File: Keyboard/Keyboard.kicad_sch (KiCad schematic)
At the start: 134 parts, among them SW1 Escape, SW10 8/*, SW11 9/(, SW12 0/), SW13 -/_, SW14 =/+, SW15 Delete, SW16 Tab, SW17 Q, SW18 W, SW19 E, SW2 `/~, SW20 R, SW21 T, SW22 Y, SW23 U, SW24 I, SW25 O, SW26 P, SW27 [/{, SW28 ]/}, SW29 \/|, SW3 1/!, SW30 Caps, SW31 A, SW32 S, SW33 D, SW34 F, SW35 G, SW36 H, SW37 J, SW38 K, SW39 L, SW4 2/@, SW40 ;/:, SW41 '/", SW42 Return, SW43 L Shift, SW44 Z, SW45 X, SW46 C, SW47 V, SW48 B, SW49 N, SW5 3/#, SW50 M, SW51 ,/<, SW52 ./>, SW53 //?, SW54 R Shift, SW55 L Control, SW56 L Alt, SW57 L Command, SW58 Space, SW59 R Command, SW6 4/$, SW60 R Alt, SW61 Up, SW62 Left, SW63 Down, SW64 Right, SW65 R Control, SW7 5/%, SW8 6/^, SW9 7/&

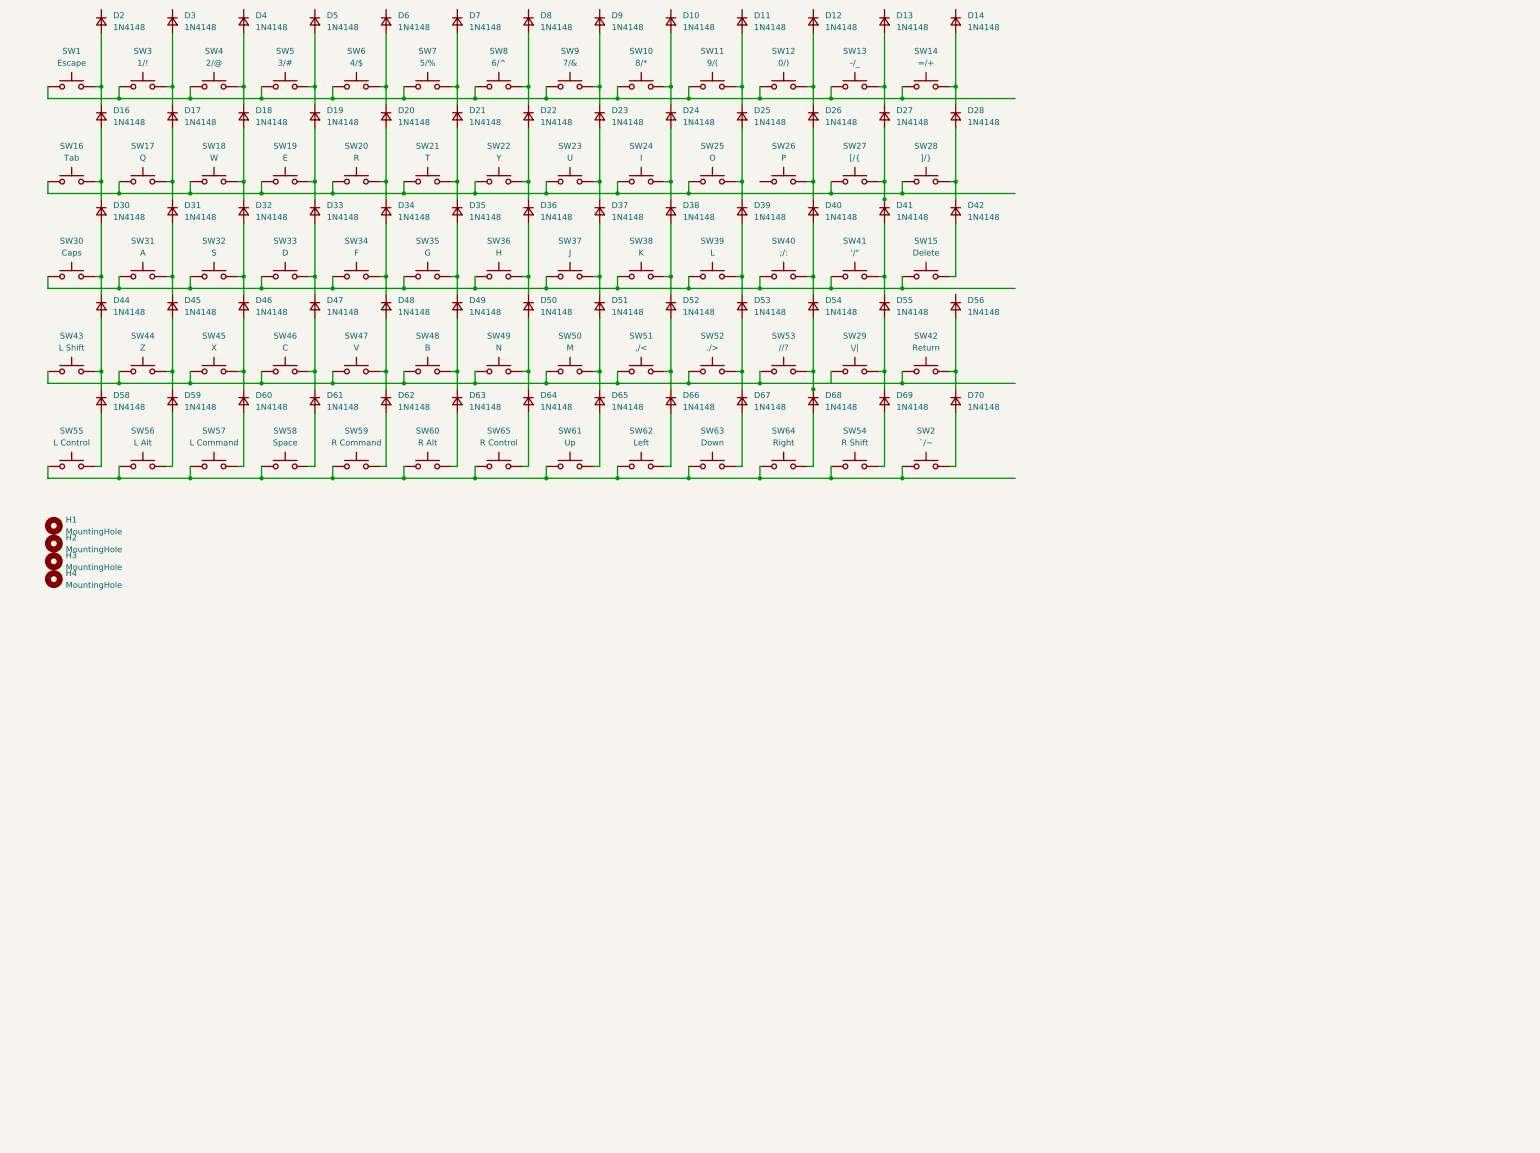
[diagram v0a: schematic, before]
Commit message: mostly updating keyboard
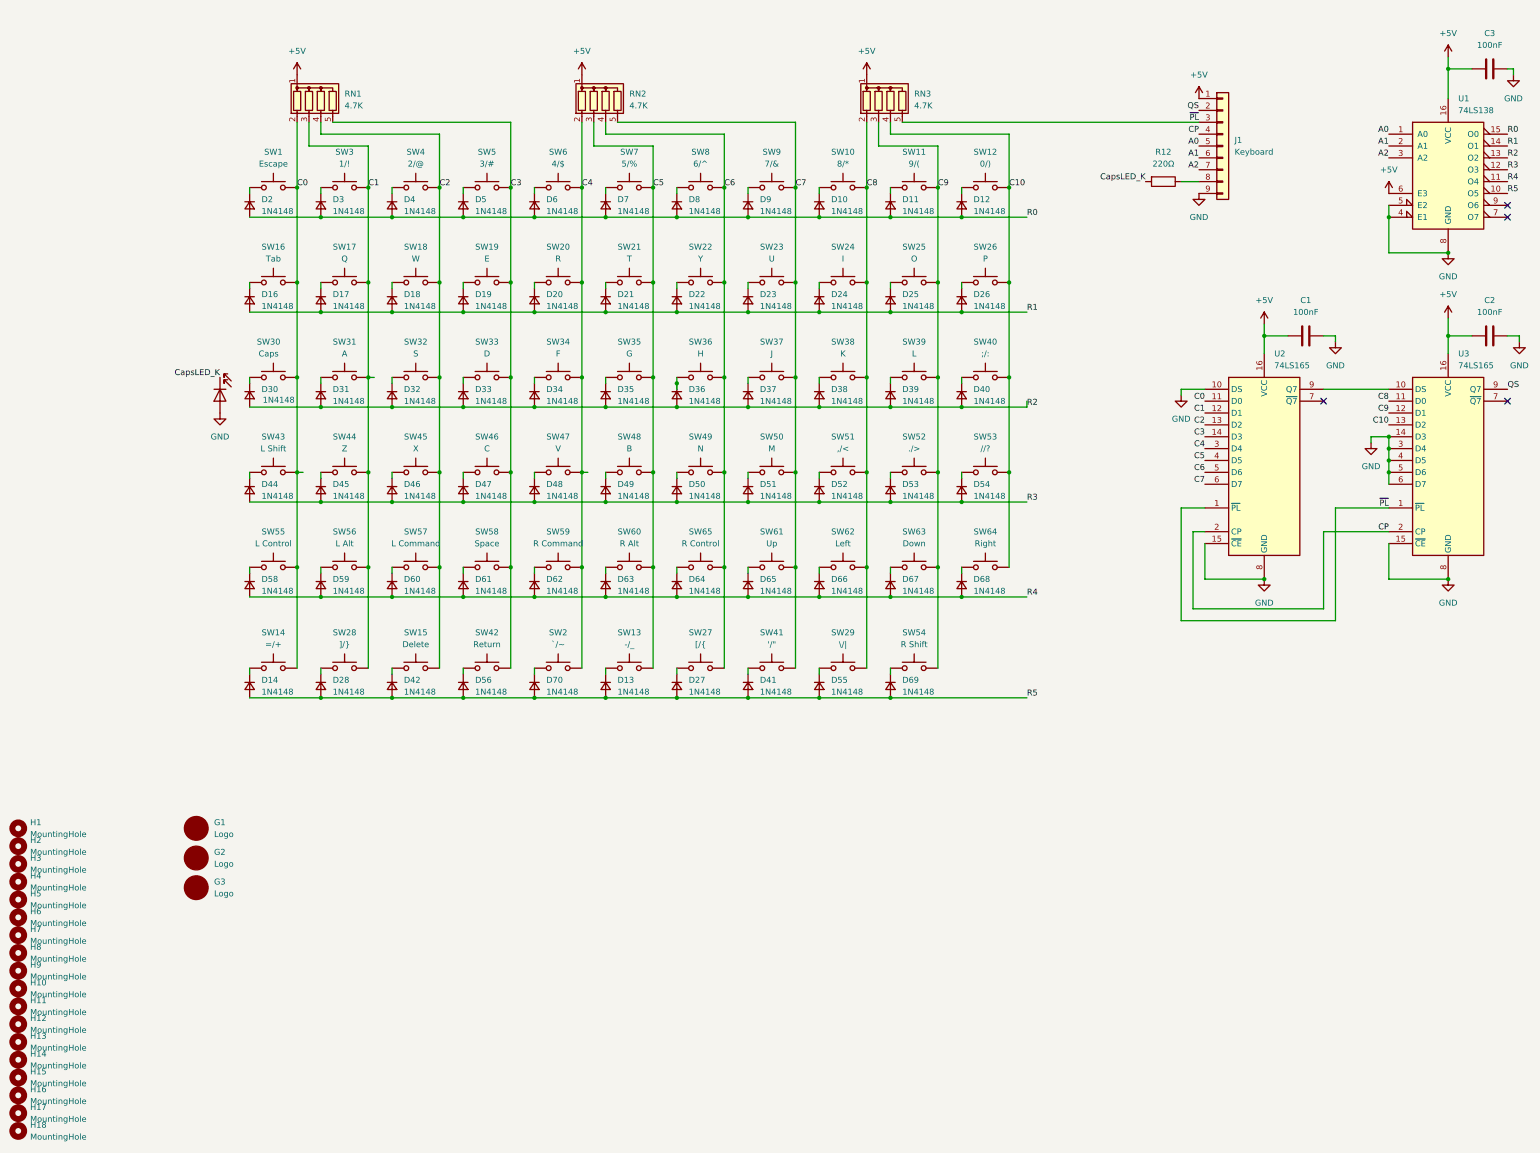
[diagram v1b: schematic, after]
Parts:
- added C1, C2, C3: 100nF, 0-Footprints:C_Disc_D5.0mm_W2.5mm_P5.00mm, symbol Device:C
- added G1: Logo, 0-Footprints:Crank, symbol 0-Symbols:Logo
- added G2: Logo, Symbol:OSHW-Logo2_7.3x6mm_SilkScreen, symbol 0-Symbols:Logo
- added G3: Logo, 0-Footprints:crankery_small, symbol 0-Symbols:Logo
- added H10, H11, H12, H13, H14, H15, H16, H17, H18, H5, H6, H7, H8, H9: MountingHole, 0-Footprints:MountingHole_2.1mm, symbol Mechanical:MountingHole
- added J1: Keyboard, 0-Footprints:PinHeader_1x09_P2.54mm_Horizontal, symbol Connector_Generic:Conn_01x09
- added R12: 220Ω, Resistor_THT:R_Axial_DIN0204_L3.6mm_D1.6mm_P7.62mm_Horizontal, symbol Device:R
- added RN1, RN2, RN3: 4.7K, Resistor_THT:R_Array_SIP5, symbol Device:R_Network04
- added U1: 74LS138, 0-Footprints:DIP-16_W7.62mm, symbol 74xx:74LS138
- added U2, U3: 74LS165, 0-Footprints:DIP-16_W7.62mm, symbol 74xx:74LS165
- D10, D11, D12, D13, D14, D16, D17, D18, D19, D2, D20, D21, D22, D23, D24, D25, D26, D27, D28, D3, D30, D31, D32, D33, D34, D35, D36, D37, D38, D39, D4, D40, D41, D42, D44, D45, D46, D47, D48, D49, D5, D50, D51, D52, D53, D54, D55, D56, D58, D59, D6, D60, D61, D62, D63, D64, D65, D66, D67, D68, D69, D7, D70, D8, D9: footprint Diode_THT:D_DO-35_SOD27_P7.62mm_Horizontal -> 0-Footprints:D_DO-35_SOD27_P7.62mm_Horizontal
- SW30: footprint 0-Footprints:SW_Cherry_MX_1.75u_PCB -> 0-Footprints:SW_Cherry_MX_1.75u_PCB_LED; symbol Switch:SW_Push -> 0-Symbols:SW_Push_LED
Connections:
- net at D3.1 (K): now also SW3.1
- net C3: now reaches SW58.2
- net C3: now also SW19.2, SW33.2, SW42.2, SW46.2, SW5.2, RN1.5 (R4), U2.14 (D3); no longer D61.2 (A)
- net at D2.1 (K): now also SW1.1
- net C9: now reaches SW63.2
- net C9: now also SW11.2, SW25.2, SW39.2, SW52.2, SW54.2, RN3.3 (R2), U3.12 (D1); no longer D67.2 (A)
- net C4: now reaches SW59.2
- net C4: now also SW2.2, SW20.2, SW34.2, SW47.2, SW6.2, RN2.2 (R1), U2.3 (D4); no longer D62.2 (A)
- net C10: now reaches SW64.2
- net C10: now also SW12.2, SW26.2, SW40.2, SW53.2, RN3.4 (R3), U3.13 (D2); no longer D68.2 (A)
- net at SW29.1: now also D55.1 (K)
- net at D56.1 (K): now also SW42.1
- net C2: now reaches SW15.2
- net C2: now also SW18.2, SW32.2, SW4.2, SW45.2, SW57.2, RN1.4 (R3), U2.13 (D2); no longer D42.2 (A)
- net C6: now reaches SW65.2
- net C6: now also SW22.2, SW27.2, SW36.2, SW49.2, SW8.2, RN2.4 (R3), U2.5 (D6); no longer D64.2 (A)
- net at D10.1 (K): now also SW10.1
- net R4: now reaches D60.2 (A)
- net R4: now also D58.2 (A), D59.2 (A), D61.2 (A), D62.2 (A), D63.2 (A), D64.2 (A), D65.2 (A), D66.2 (A), D67.2 (A), D68.2 (A), U1.11 (O4); no longer SW57.2
- net at SW26.1: now also D26.1 (K)
- net C5: now reaches SW60.2
- net C5: now also SW13.2, SW21.2, SW35.2, SW48.2, SW7.2, RN2.3 (R2), U2.4 (D5); no longer D63.2 (A)
- net C0: now reaches SW55.2
- net C0: now also SW1.2, SW14.2, SW16.2, SW30.2, SW43.2, RN1.2 (R1), U2.11 (D0); no longer D58.2 (A)
- net at D7.1 (K): now also SW7.1
- net at D14.1 (K): now also SW14.1
- net R5: now reaches D70.2 (A)
- net R5: now also D13.2 (A), D14.2 (A), D27.2 (A), D28.2 (A), D41.2 (A), D42.2 (A), D55.2 (A), D56.2 (A), D69.2 (A), U1.10 (O5); no longer SW2.2
- net at D12.1 (K): now also SW12.1
- net C7: now reaches SW61.2
- net C7: now also SW23.2, SW37.2, SW41.2, SW50.2, SW9.2, RN2.5 (R4), U2.6 (D7); no longer D65.2 (A)
- net at D11.1 (K): now also SW11.1
- net C8: now reaches SW62.2
- net C8: now also SW10.2, SW24.2, SW29.2, SW38.2, SW51.2, RN3.2 (R1), U3.11 (D0); no longer D66.2 (A)
- net at D8.1 (K): now also SW8.1
- net C1: now reaches SW56.2
- net C1: now also SW17.2, SW28.2, SW3.2, SW31.2, SW44.2, RN1.3 (R2), U2.12 (D1); no longer D59.2 (A)
- net at D13.1 (K): now also SW13.1
- net at D4.1 (K): now also SW4.1
- net at D6.1 (K): now also SW6.1
- net at D9.1 (K): now also SW9.1
- net at D5.1 (K): now also SW5.1
- new net: D19.1 (K), SW19.1
- new net: D34.1 (K), SW34.1
- new net: D54.1 (K), SW53.1
- new net: D44.1 (K), SW43.1
- new net: D61.1 (K), SW58.1
- new net: D18.1 (K), SW18.1
- new net: D36.1 (K), SW36.1
- new net: D53.1 (K), SW52.1
- new net: D40.1 (K), SW40.1
- new net: D38.1 (K), SW38.1
- new net: D67.1 (K), SW63.1
- new net: D62.1 (K), SW59.1
- new net: D68.1 (K), SW64.1
- new net: D45.1 (K), SW44.1
- new net: D50.1 (K), SW49.1
- new net: D42.1 (K), SW15.1
- new net: D20.1 (K), SW20.1
- new net: D48.1 (K), SW47.1
- new net: D46.1 (K), SW45.1
- new net: D64.1 (K), SW65.1
- new net: D39.1 (K), SW39.1
- new net: D35.1 (K), SW35.1
- new net: D17.1 (K), SW17.1
- new net: D47.1 (K), SW46.1
- new net: D41.1 (K), SW41.1
- new net: D60.1 (K), SW57.1
- new net: D24.1 (K), SW24.1
- new net: D63.1 (K), SW60.1
- new net: D32.1 (K), SW32.1
- new net: D16.1 (K), SW16.1
- new net: D25.1 (K), SW25.1
- new net: D58.1 (K), SW55.1
- new net: D27.1 (K), SW27.1
- new net: D30.1 (K), SW30.1
- new net: D21.1 (K), SW21.1
- new net: D33.1 (K), SW33.1
- new net: U2.9 (Q7), U3.10 (DS)
- new net: D51.1 (K), SW50.1
- new net: D52.1 (K), SW51.1
- new net: D49.1 (K), SW48.1
- new net: D70.1 (K), SW2.1
- new net: D69.1 (K), SW54.1
- new net: D28.1 (K), SW28.1
- new net: D65.1 (K), SW61.1
- new net: D31.1 (K), SW31.1
- new net: D37.1 (K), SW37.1
- new net: D66.1 (K), SW62.1
- new net: J1.8 (Pin_8), R12.1
- new net: D59.1 (K), SW56.1
- new net: D23.1 (K), SW23.1
- new net: D22.1 (K), SW22.1
- new net +5V: C1.2, C2.2, C3.2, J1.1 (Pin_1), RN1.1 (common), RN2.1 (common), RN3.1 (common), U1.16 (VCC), U1.6 (E3), U2.16 (VCC), U3.16 (VCC)
- new net A0: J1.5 (Pin_5), U1.1 (A0)
- new net A1: J1.6 (Pin_6), U1.2 (A1)
- new net A2: J1.7 (Pin_7), U1.3 (A2)
- new net CP: J1.4 (Pin_4), U2.2 (CP), U3.2 (CP)
- new net CapsLED_K: R12.2, SW30.3 (K)
- new net GND: C1.1, C2.1, C3.1, J1.9 (Pin_9), SW30.4 (A), U1.4 (E1), U1.5 (E2), U1.8 (GND), U2.10 (DS), U2.15 (~{CE}), U2.8 (GND), U3.14 (D3), U3.15 (~{CE}), U3.3 (D4), U3.4 (D5), U3.5 (D6), U3.6 (D7), U3.8 (GND)
- new net QS: J1.2 (Pin_2), U3.9 (Q7)
- new net R0: D10.2 (A), D11.2 (A), D12.2 (A), D2.2 (A), D3.2 (A), D4.2 (A), D5.2 (A), D6.2 (A), D7.2 (A), D8.2 (A), D9.2 (A), U1.15 (O0)
- new net R1: D16.2 (A), D17.2 (A), D18.2 (A), D19.2 (A), D20.2 (A), D21.2 (A), D22.2 (A), D23.2 (A), D24.2 (A), D25.2 (A), D26.2 (A), U1.14 (O1)
- new net R2: D30.2 (A), D31.2 (A), D32.2 (A), D33.2 (A), D34.2 (A), D35.2 (A), D36.2 (A), D37.2 (A), D38.2 (A), D39.2 (A), D40.2 (A), U1.13 (O2)
- new net R3: D44.2 (A), D45.2 (A), D46.2 (A), D47.2 (A), D48.2 (A), D49.2 (A), D50.2 (A), D51.2 (A), D52.2 (A), D53.2 (A), D54.2 (A), U1.12 (O3)
- new net ~{PL}: J1.3 (Pin_3), RN3.5 (R4), U2.1 (~{PL}), U3.1 (~{PL})
- no-connect marks 0 -> 4
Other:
- moved on the sheet: D10, D11, D12, D13, D14, D16, D17, D18, D19, D2, D20, D21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
